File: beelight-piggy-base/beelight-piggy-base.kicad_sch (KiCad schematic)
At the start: 76 parts, among them J1 B_Le, J2 B_Ri, J3 USB_C_Receptacle_PowerOnly_6P, J4 WS2812_ext, J5 PROG, J6 BatSide, J7 DevSide, Q1 AO3400A, SW1 BOOT, U1 MCP73871, U2 BMA253, U3 TPS22917LDBV, U4 ADS1115IDGS, U5 VEML3328, U6 TSOP382xx

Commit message: first final proto
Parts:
- removed J5: PROG, Connector_PinHeader_2.54mm:PinHeader_1x06_P2.54mm_Vertical_SMD_Pin1Right, symbol Connector:Conn_01x06_Pin
- removed JP10, JP11, JP12, JP13, JP14, JP15, JP16, JP17, JP18, JP2, JP3, JP4, JP5, JP6, JP7, JP8, JP9: jpd, symbol Jumper:SolderJumper_2_Open
- removed R4: 220k, symbol Device:R_Small
- removed SW1: BOOT, Button_Switch_SMD:SW_Tactile_SPST_NO_Straight_CK_PTS636Sx25SMTRLFS, symbol Switch:SW_Push
- removed U4: ADS1115IDGS, Package_SO:TSSOP-10_3x3mm_P0.5mm, symbol Analog_ADC:ADS1115IDGS
- added C10, C11, C12, C13, C14, C15, C16, C17, C18, C19, C20, C21, C5, C6, C7, C8, C9: 100n, Capacitor_SMD:C_0402_1005Metric, symbol Device:C_Small
- added C22: 100µF, Capacitor_SMD:C_1210_3225Metric, symbol Device:C_Polarized
- added J5: Conn_01x07_Pin, Connector_PinSocket_2.54mm:PinSocket_1x07_P2.54mm_Vertical, symbol Connector:Conn_01x07_Pin
- added J8: B_Ri, Connector_PinHeader_2.54mm:PinHeader_1x10_P2.54mm_Vertical, symbol Connector_Generic:Conn_01x10
- added J9: B_Le, Connector_PinHeader_2.54mm:PinHeader_1x10_P2.54mm_Vertical, symbol Connector_Generic:Conn_01x10
- added R15: 20k, Resistor_SMD:R_0805_2012Metric, symbol Device:R_Small
- added R16: 40k, Resistor_SMD:R_0805_2012Metric, symbol Device:R_Small
- added R17: 4k7, Resistor_SMD:R_0805_2012Metric, symbol Device:R_Small
- C1, C2, C3: footprint (none) -> Capacitor_SMD:C_1210_3225Metric
- C4: value 100nF -> 100n; footprint (none) -> Capacitor_SMD:C_0402_1005Metric
- D17, D18, D19: footprint (none) -> LED_SMD:LED_0201_0603Metric
- F1: footprint (none) -> Fuse:Fuse_1812_4532Metric
- J1, J2: footprint Connector_PinHeader_2.54mm:PinHeader_1x09_P2.54mm_Vertical -> Connector_PinHeader_2.54mm:PinHeader_1x10_P2.54mm_Vertical
- J3: footprint Connector_USB:USB_C_Receptacle_GCT_USB4105-xx-A_16P_TopMnt_Horizontal -> Connector_USB:USB_C_Receptacle_GCT_USB4125-xx-x-0190_6P_TopMnt_Horizontal
- J4: footprint Connector_Harwin:Harwin_M20-89003xx_1x03_P2.54mm_Horizontal -> Connector_JST:JST_GH_SM03B-GHS-TB_1x03-1MP_P1.25mm_Horizontal
- J7: footprint (none) -> Connector_JST:JST_GH_SM02B-GHS-TB_1x02-1MP_P1.25mm_Horizontal
- JP1: value jpd -> bypass_ws; footprint (none) -> Jumper:SolderJumper-2_P1.3mm_Open_RoundedPad1.0x1.5mm
- R1, R11, R12, R13, R14, R2, R3, R5, R6, R7, R8, R9: footprint (none) -> Resistor_SMD:R_0805_2012Metric
- R10: value 100k -> 10k; footprint (none) -> Resistor_SMD:R_0805_2012Metric
- TH1: footprint Resistor_SMD:R_2816_7142Metric_Pad3.20x4.45mm_HandSolder -> Resistor_SMD:R_0805_2012Metric
- U5: footprint VEML3328:VEML3328 -> beelight:VEML3328
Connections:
- net +3.3V: now also J2.2 (+3V3), J5.3 (Pin_3), J8.2 (+3V3); no longer J2.+3V3 (Pin_2)
- net +5VP: now also J1.3 (REG), J9.3 (REG); no longer J1.REG (Pin_8)
- net GND: now also C4.2, J1.1 (GND), J1.2 (GND), C10.2, C11.2, C12.2, C13.2, C14.2, C15.2, C16.2, C17.2, C18.2, C19.2, C20.2, C21.2, C22.2, C5.2, C6.2, C7.2, C8.2, C9.2, J5.2 (Pin_2), J9.1 (GND), J9.2 (GND), R17.1; no longer C4.1, J1.GND (Pin_10), R10.2
- net VLED: now also C4.1, C10.1, C11.1, C12.1, C13.1, C14.1, C15.1, C16.1, C17.1, C18.1, C19.1, C20.1, C21.1, C22.1, C5.1, C6.1, C7.1, C8.1, C9.1
- net at U2.12 (SCK/SCL), U5.3 (SCL): now also J1.6 (SCL), J9.6 (SCL); no longer J1.SCL (Pin_5)
- net at U3.3 (~{ON}): now also J1.5 (SCL2), J9.5 (SCL2); no longer J1.SCL2 (Pin_6)
- net at R14.1: now also J1.8 (TXD), J5.6 (Pin_6), J9.8 (TXD); no longer J1.SCLP (Pin_7)
- net at U2.2 (SDI/SDA), U5.2 (SDA): now also J1.7 (SDA), J5.7 (Pin_7), J9.7 (SDA); no longer J1.SDA (Pin_4)
- net at D18.1 (K), R6.2: now also R15.1
- net at D1.3 (DIN), R3.2: now also JP1.2 (B); no longer JP1.1 (A)
- net at D1.1 (DOUT), D2.3 (DIN): no longer JP1.2 (B)
- net at D22.1 (DOUT), J4.2 (Pin_2): now also JP1.1 (A)
- net at R13.1: now also Q1.1 (G), R14.2
- net at U6.1 (OUT): now also J1.4 (SCLP), J9.4 (SCLP); no longer J2.ADC (Pin_3)
- net at R3.1: now also J2.9 (BUZ), J8.9 (BUZ); no longer J2.BUZ (Pin_9)
- net at R10.1: now also D17.1 (K), R5.2; no longer C4.2
- net at D19.1 (K), R7.2: now also R16.1
- new net: J1.10 (EN), J5.1 (Pin_1), J9.10 (EN)
- new net: J1.9 (RXD), J5.5 (Pin_5), J9.9 (RXD)
- new net: J2.3 (ADC), J8.3 (ADC), R10.2, R15.2, R16.2, R17.2
- new net: J2.6 (RST), J5.4 (Pin_4), J8.6 (RST)
- no-connect marks 12 -> 13
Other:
- note removed: "A/D"
- moved on the sheet: J2, R3

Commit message: add rysta symbol to schematic
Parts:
- added U4: rysta, beelight:rysta, symbol .local:rysta
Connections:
- net +3.3V: now also U4.2 (+3.3V)
- net +5VP: now also U4.1 (+5V)
- net GND: now also U4.19 (GND), U4.20 (GND)
- net at R10.2, R15.2, R16.2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: no longer J2.3 (ADC), J8.3 (ADC)
- new net: J2.3 (ADC), J8.3 (ADC)
- new net IR_RX: U4.16 (SCL2)
- new net IR_TX: U4.17 (SCLP)
- new net RST: U4.6 (RST)
- new net SCL: U4.9 (BUZ)
- new net SDA: U4.14 (SDA)
- new net TXD: U4.13 (TXD)
- new net WAKE: U4.5 (WAKE)
- no-connect marks 13 -> 15
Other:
- note added: "GPIO0"
- note added: "GPIO16"
- note added: "GPIO2"
- note added: "GPIO4"
- note added: "GPIO5"
- note added: "GPIO9"
- moved on the sheet: BT1, C1, C2, C3, D17, D18, D19, J3, J6, J7, R1, R10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

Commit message: rewire existing components
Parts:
- added C23: 100n, symbol .local:C
- added D23: D_Schottky, symbol .local:D_Schottky
- added R4: 100k, symbol Device:R_Small
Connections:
- net +5VP: now also R4.1; no longer R12.2
- net GND: now also C23.2
- net IR_RX: now also U6.1 (OUT)
- net IR_TX: now also R14.1
- net RST: now also J5.4 (Pin_4)
- net RXD: now also J5.5 (Pin_5)
- net SCL: now also U2.12 (SCK/SCL), U5.3 (SCL)
- net SDA: now also J5.7 (Pin_7), U2.2 (SDI/SDA), U5.2 (SDA)
- net TXD: now also J5.6 (Pin_6), D23.2 (A)
- net VLED: now also R12.2
- net WS_DATA: now also R3.2
- net at J1.10 (EN), J9.10 (EN): no longer J5.1 (Pin_1)
- net at J1.4 (SCLP), J9.4 (SCLP): no longer U6.1 (OUT)
- net at J1.5 (SCL2), J9.5 (SCL2): no longer U3.3 (~{ON})
- net at J1.6 (SCL), J9.6 (SCL): no longer U2.12 (SCK/SCL), U5.3 (SCL)
- net at J1.8 (TXD), J9.8 (TXD): no longer J5.6 (Pin_6), R14.1
- net at J1.9 (RXD), J9.9 (RXD): no longer J5.5 (Pin_5)
- net at D1.3 (DIN), JP1.2 (B): now also R3.1; no longer R3.2
- net at J2.6 (RST), J8.6 (RST): no longer J5.4 (Pin_4)
- net at J2.9 (BUZ), J8.9 (BUZ): no longer R3.1
- new net: J1.7 (SDA), J9.7 (SDA)
- new net: C23.1, D23.1 (K), R4.2, U3.3 (~{ON})
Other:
- moved on the sheet: D20, F1, Q1, R11, R12, R13, R14, R3, U3, U6

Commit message: add replace power and charge section
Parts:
- removed C2, C3: 4.7µF, Capacitor_SMD:C_1210_3225Metric, symbol Device:C_Polarized_Small
- removed D17, D18, D19: LED_Small, LED_SMD:LED_0201_0603Metric, symbol Device:LED_Small
- removed R10: 10k, Resistor_SMD:R_0805_2012Metric, symbol Device:R_Small
- removed R15: 20k, Resistor_SMD:R_0805_2012Metric, symbol Device:R_Small
- removed R16: 40k, Resistor_SMD:R_0805_2012Metric, symbol Device:R_Small
- removed R17: 4k7, Resistor_SMD:R_0805_2012Metric, symbol Device:R_Small
- removed R5, R6, R7, R8, R9: 470R, Resistor_SMD:R_0805_2012Metric, symbol Device:R_Small
- removed U1: MCP73871, Package_DFN_QFN:QFN-20-1EP_4x4mm_P0.5mm_EP2.5x2.5mm, symbol Battery_Management:MCP73871
- added C25: 0.1uF, .local:C_0402_1005Metric, symbol .local:C
- added C26: 10uF, .local:C_0805_2012Metric, symbol .local:C
- added C27: 1uF, .local:C_0402_1005Metric, symbol .local:C
- added C28: 1uF, .local:C_0603_1608Metric, symbol .local:C
- added C29: 2.2uF, .local:C_0603_1608Metric, symbol .local:C
- added D24, D25: D_Schottky, symbol .local:D_Schottky
- added R18: 200k, .local:R_0402_1005Metric, symbol .local:R
- added R19, R20: 10k, .local:R_0402_1005Metric, symbol .local:R
- added R21, R22: 100k, .local:R_0402_1005Metric, symbol .local:R
- added U7: MP2667, .local:QFN-10_2x2mm_P0.5mm, symbol .local:MP2667
- added U8: BQ27421-G1, .local:BGA-9_1.6x1.6mm_Layout3x3_P0.5mm, symbol .local:BQ27421-G1
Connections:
- net +5VP: now also C29.1, U7.10 (SYS)
- net GND: now also C25.2, C26.2, C27.2, C28.2, C29.2, R20.2, R22.2, U7.5 (GND), U8.B2 (VSS), U8.C1 (VSS)
- net RST: now also D25.2 (A)
- net SCL: now also U7.6 (SCL), U8.A3 (SCL)
- net SDA: now also U7.7 (SDA), U8.A2 (SDA)
- net VBUS: now also R21.1, U7.1 (IN)
- net WAKE: now also D24.2 (A)
- net BAT: now reaches J7.2 (Pin_2)
- net BAT: now also C28.1, U8.C3 (BAT)
- net NTC: now reaches TH1.1
- net NTC: now also R21.2, R22.1, U7.2 (NTC)
- new net: D24.1 (K), R18.2, U7.3 (INT)
- new net: C25.1, R18.1, U7.4 (VDD)
- new net: C26.1, U7.8 (BATT), U7.9 (BATT), U8.C2 (SRX)
- new net: D25.1 (K), R19.2, U8.A1 (GPOUT)
- new net: R20.1, U8.B1 (BIN)
- new net: C27.1, R19.1, U8.B3 (VDD)
- no-connect marks 15 -> 14
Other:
- note added: "LED"
- note removed: "LEDs"
- moved on the sheet: C1, C10, C11, C12, C13, C14, C15, C16, C17, C18, C19, C20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

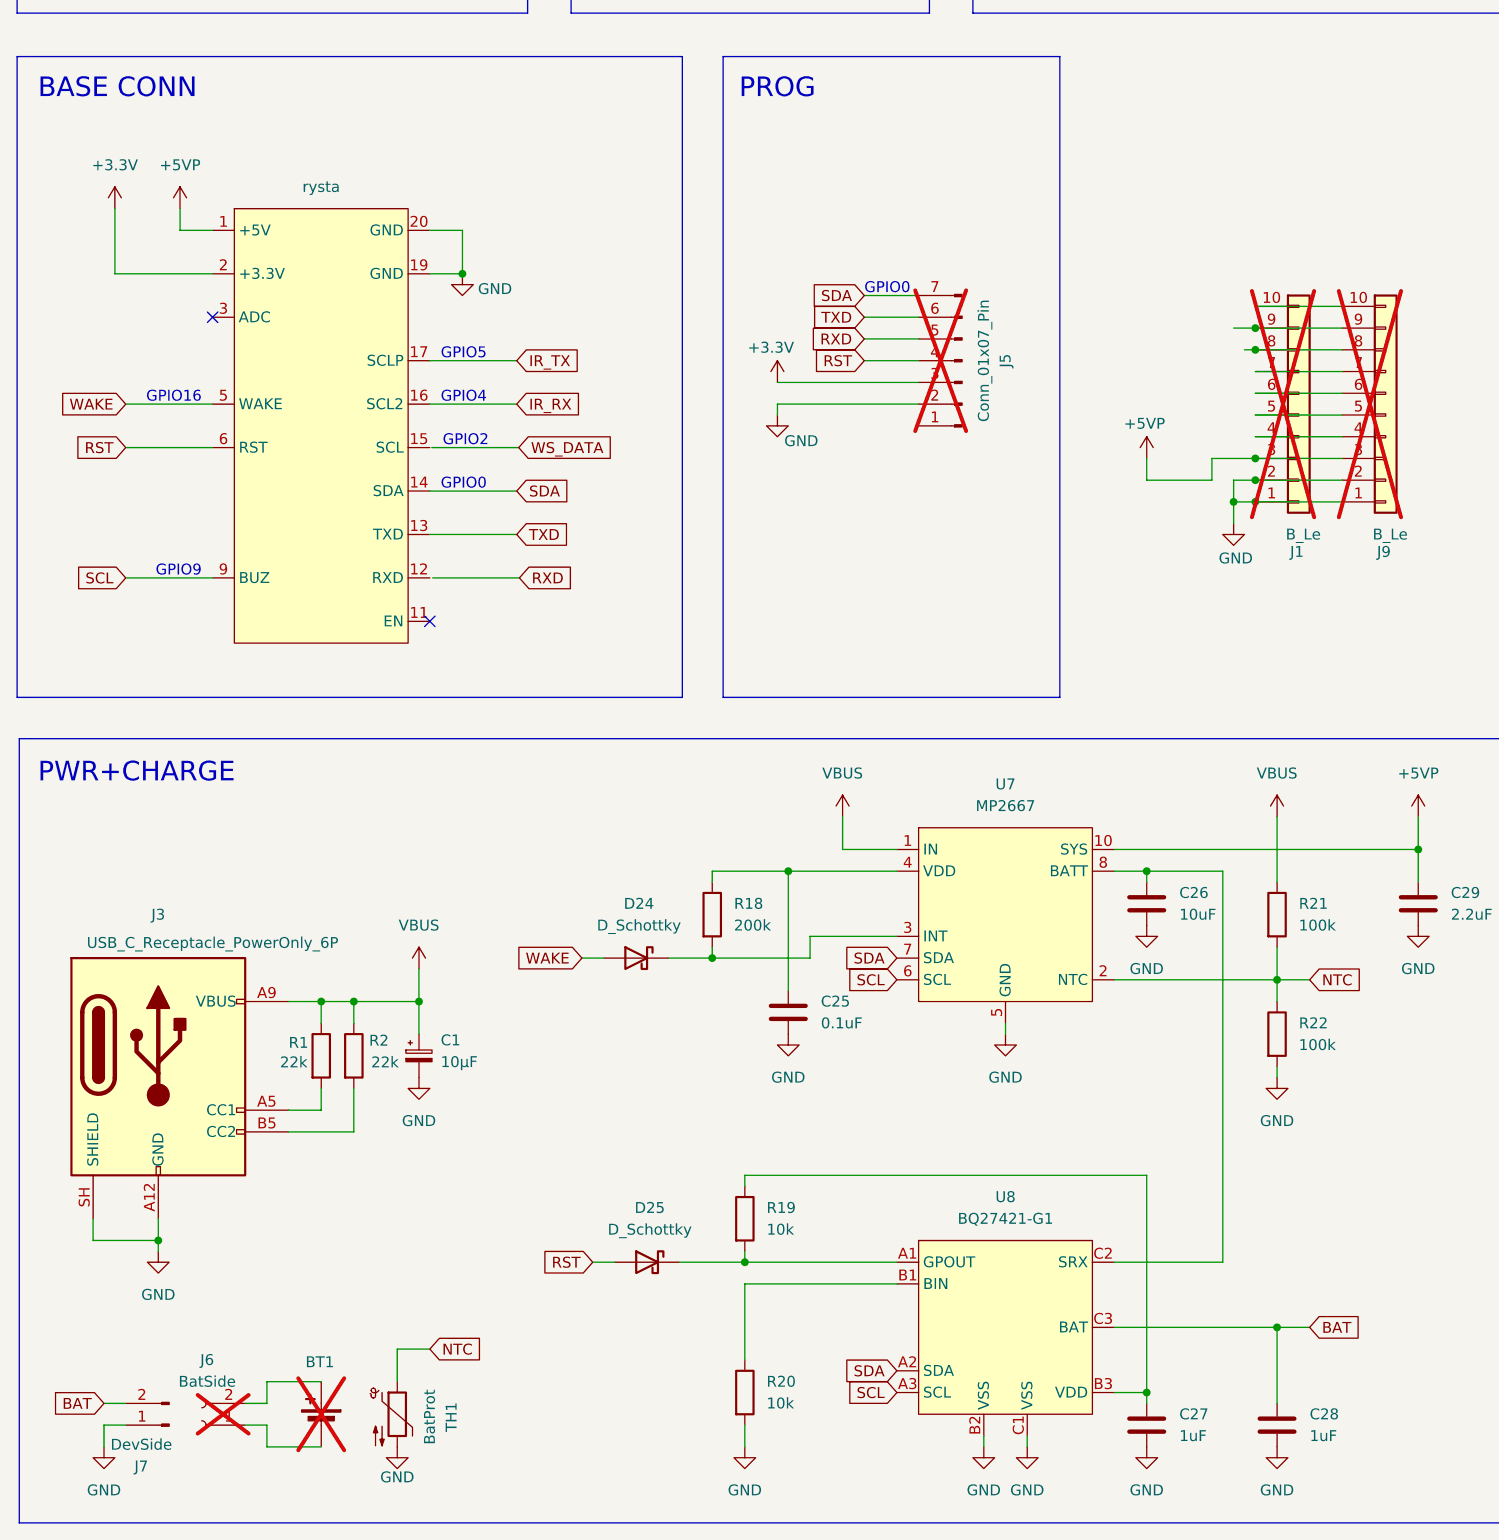
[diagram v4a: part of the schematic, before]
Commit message: add pull-up for SCL, change gpout pull-up connection and add wake button
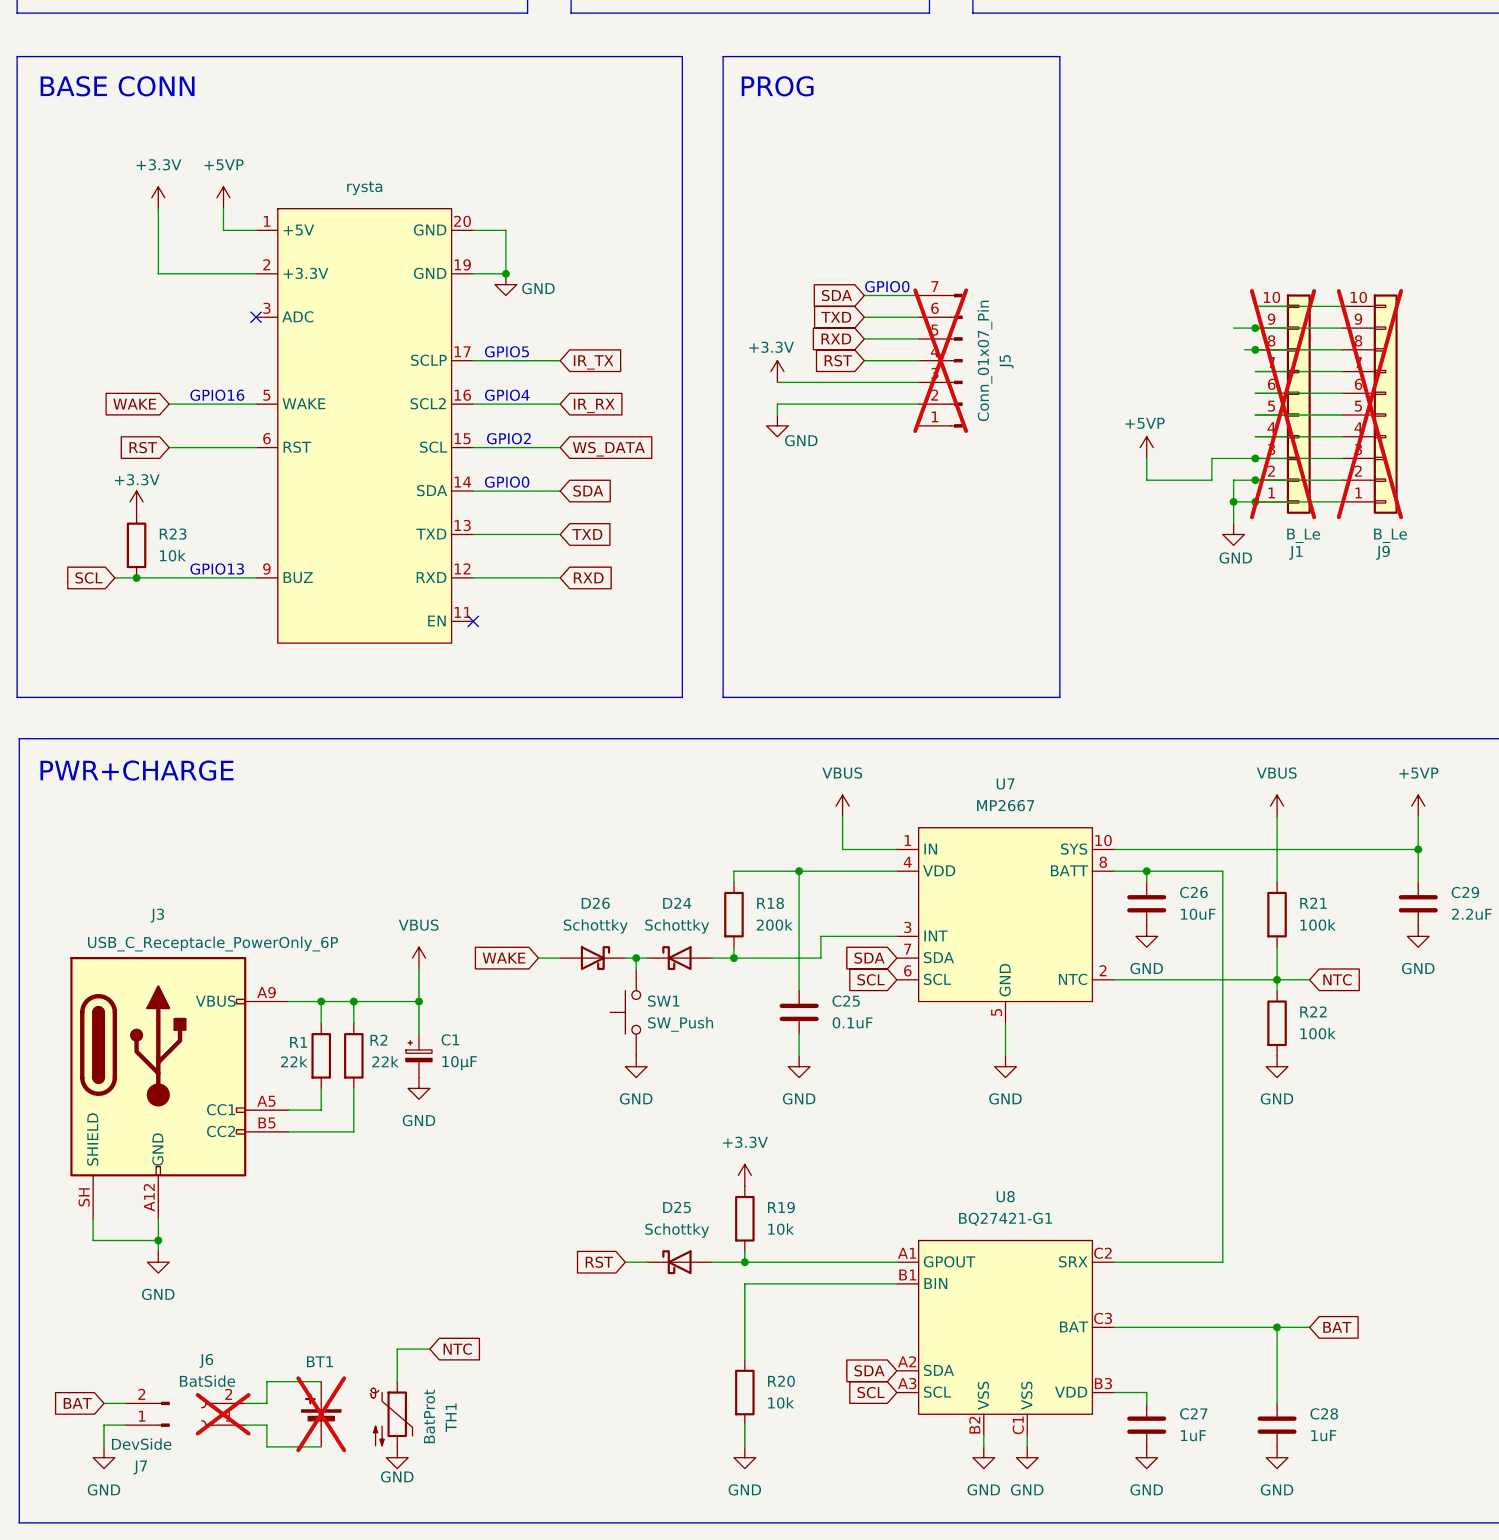
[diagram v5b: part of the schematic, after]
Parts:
- added D26: Schottky, symbol .local:D_Schottky
- added R23: 10k, .local:R_0402_1005Metric, symbol .local:R
- added SW1: SW_Push, symbol .local:SW_Push
- D24, D25: value D_Schottky -> Schottky
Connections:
- net +3.3V: now also R19.1, R23.1
- net GND: now also SW1.1
- net RST: now also D25.1 (K); no longer D25.2 (A)
- net RXD: now also U4.12 (RXD)
- net SCL: now also R23.2
- net WAKE: now also D26.2 (A); no longer D24.2 (A)
- net WS_DATA: now also U4.15 (SCL)
- net at R18.2, U7.3 (INT): now also D24.2 (A); no longer D24.1 (K)
- net at R19.2, U8.A1 (GPOUT): now also D25.2 (A); no longer D25.1 (K)
- net at C27.1, U8.B3 (VDD): no longer R19.1
- new net: D24.1 (K), D26.1 (K), SW1.2
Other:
- note added: "GPIO13"
- note removed: "GPIO9"
- moved on the sheet: C25, D24, D25, R18, R22

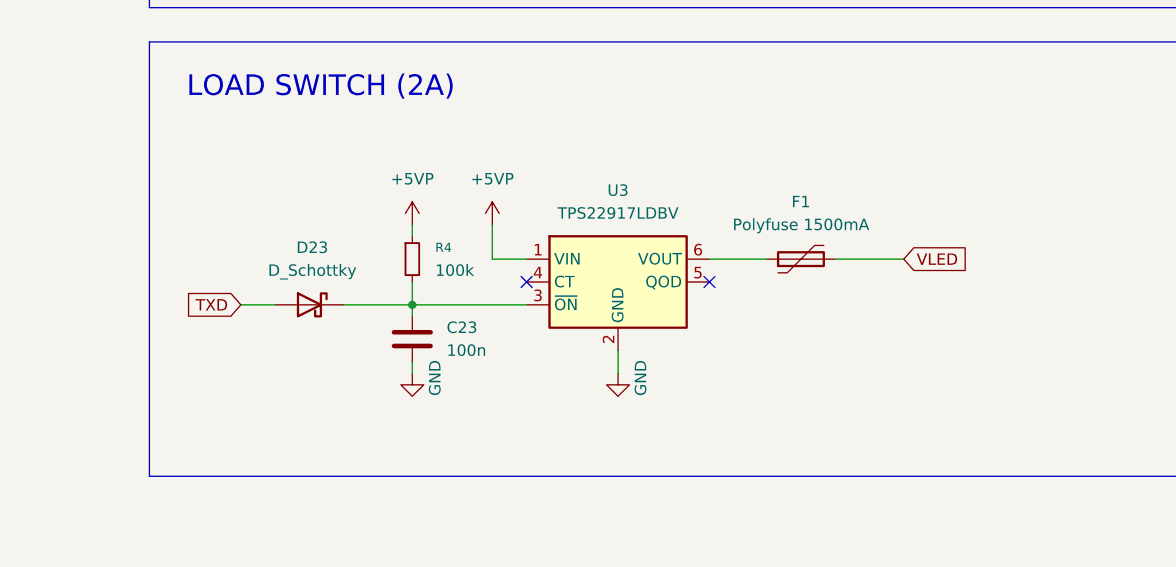
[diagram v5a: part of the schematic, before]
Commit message: use WS_DATA for load switch
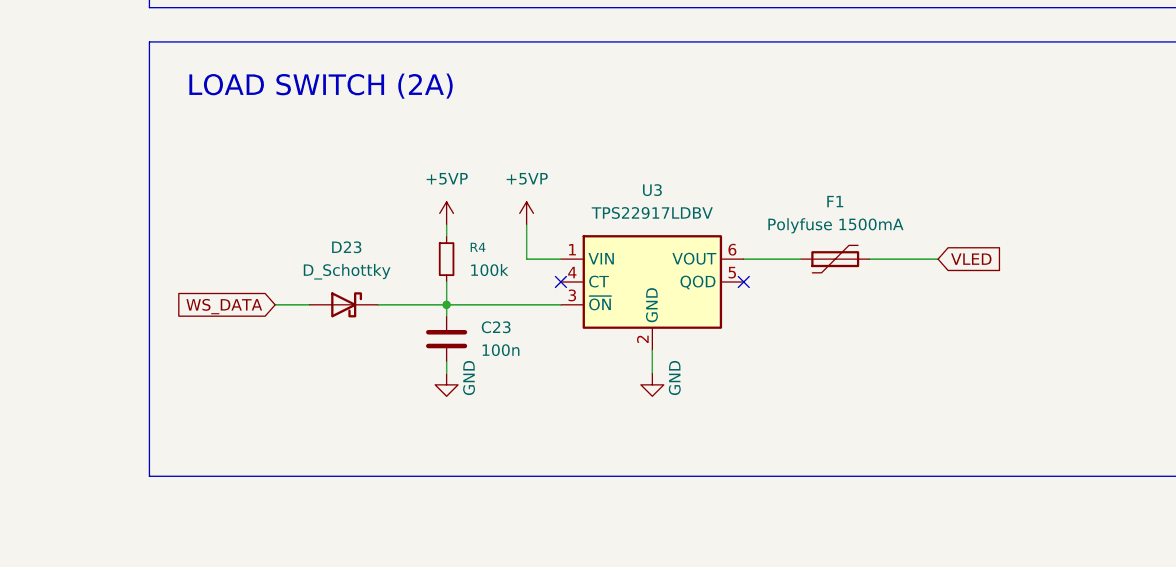
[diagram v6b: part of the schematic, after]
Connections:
- net TXD: no longer D23.2 (A)
- net WS_DATA: now also D23.2 (A)
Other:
- moved on the sheet: C23, D23, F1, R4, U3

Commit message: fix D23 orientation
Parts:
- D23: value D_Schottky -> Schottky
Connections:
- net WS_DATA: now also D23.1 (K); no longer D23.2 (A)
- net at C23.1, R4.2, U3.3 (~{ON}): now also D23.2 (A); no longer D23.1 (K)
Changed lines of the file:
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@@
 		(property "Value" "SW_Push"
 			(at 96.52 198.1199 90)
+			(hide yes)
 			(show_name no)
 			(do_not_autoplace no)
@@
 		(lib_id ".local:D_Schottky")
 		(at 256.54 226.06 0)
-		(mirror y)
 		(unit 1)
 		(body_style 1)
@@
 		(in_pos_files yes)
 		(dnp no)
-		(fields_autoplaced yes)
 		(property "Reference" "D23"
-			(at 256.8575 219.71 0)
+			(at 256.2225 219.71 0)
 			(show_name no)
 			(do_not_autoplace no)
@@
 			)
 		)
-		(property "Value" "D_Schottky"
-			(at 256.8575 222.25 0)
+		(property "Value" "Schottky"
+			(at 256.2225 222.25 0)
 			(show_name no)
 			(do_not_autoplace no)
